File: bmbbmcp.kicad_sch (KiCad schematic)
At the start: 20 parts, among them J1 USB_OTG, J2 Conn_ARM_SWD_TagConnect_TC2030, J3 Conn_01x04_Socket, U1 MDBT50Q-1MV2, U2 AP2112K-3.3, Y1 32.768

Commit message: Adding parts and gerber files from JLCPCB plugin
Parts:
- C1, C6, C7: LCSC (none) -> C15850
- C2, C5: LCSC (none) -> C14663
- C3, C4: LCSC (none) -> C1653
- D1, D2: LCSC (none) -> C130880
- J1: LCSC (none) -> C136001
- R1: LCSC (none) -> C25804
- R2: LCSC (none) -> C23345
- S1, S2: LCSC (none) -> C99271
- U1: LCSC (none) -> C5118826
- U2: LCSC (none) -> C51118
- Y1: LCSC (none) -> C620155
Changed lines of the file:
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@@
 			)
 		)
+		(property "LCSC" "C14663"
+			(at 39.37 177.7999 0)
+			(effects
+				(font
+					(size 1.27 1.27)
+				)
+				(hide yes)
+			)
+		)
 		(pin "2"
 		)
@@
 			)
 		)
+		(property "LCSC" "C136001"
+			(at 156.21 125.73 0)
+			(effects
+				(font
+					(size 1.27 1.27)
+				)
+				(hide yes)
+			)
+		)
 		(pin "6"
 		)
@@
 			)
 		)
+		(property "LCSC" "C14663"
+			(at 52.07 177.7999 0)
+			(effects
+				(font
+					(size 1.27 1.27)
+				)
+				(hide yes)
+			)
+		)
 		(pin "2"
 		)
@@
 			)
 		)
+		(property "LCSC" "C25804"
+			(at 102.87 181.6099 0)
+			(effects
+				(font
+					(size 1.27 1.27)
+				)
+				(hide yes)
+			)
+		)
 		(pin "1"
 		)
@@
 			)
 		)
+		(property "LCSC" "C23345"
+			(at 170.18 133.604 0)
+			(effects
+				(font
+					(size 1.27 1.27)
+				)
+				(hide yes)
+			)
+		)
 		(pin "2"
 		)
@@
 			)
 		)
+		(property "LCSC" "C15850"
+			(at 91.44 181.6099 0)
+			(effects
+				(font
+					(size 1.27 1.27)
+				)
+				(hide yes)
+			)
+		)
 		(pin "1"
 		)
@@
 			)
 		)
+		(property "LCSC" "C99271"
+			(at 149.86 64.77 0)
+			(effects
+				(font
+					(size 1.27 1.27)
+				)
+				(hide yes)
+			)
+		)
 		(pin "2"
 		)
@@
 			)
 		)
+		(property "LCSC" "C99271"
+			(at 149.86 85.09 0)
+			(effects
+				(font
+					(size 1.27 1.27)
+				)
+				(hide yes)
+			)
+		)
 		(pin "2"
 		)
@@
 			)
 		)
+		(property "LCSC" "C15850"
+			(at 132.08 181.6099 0)
+			(effects
+				(font
+					(size 1.27 1.27)
+				)
+				(hide yes)
+			)
+		)
 		(pin "1"
 		)
@@
 			)
 		)
+		(property "LCSC" "C15850"
+			(at 26.67 177.7999 0)
+			(effects
+				(font
+					(size 1.27 1.27)
+				)
+				(hide yes)
+			)
+		)
 		(pin "1"
 		)
@@
 			)
 		)
+		(property "LCSC" "C1653"
+			(at 99.06 53.594 0)
+			(effects
+				(font
+					(size 1.27 1.27)
+				)
+				(hide yes)
+			)
+		)
 		(pin "1"
 		)
@@
 			)
 		)
+		(property "LCSC" "C1653"
+			(at 98.806 35.306 0)
+			(effects
+				(font
+					(size 1.27 1.27)
+				)
+				(hide yes)
+			)
+		)
 		(pin "1"
 		)
@@
 			)
 		)
+		(property "LCSC" "C130880"
+			(at 81.5975 170.18 0)
+			(effects
+				(font
+					(size 1.27 1.27)
+				)
+				(hide yes)
+			)
+		)
 		(pin "1"
 		)
@@
 			)
 		)
+		(property "LCSC" "C620155"
+			(at 87.376 37.592 0)
+			(effects
+				(font
+					(size 1.27 1.27)
+				)
+				(hide yes)
+			)
+		)
 		(pin "1"
 		)
@@
 			)
 		)
+		(property "LCSC" "C130880"
+			(at 90.17 169.2274 0)
+			(effects
+				(font
+					(size 1.27 1.27)
+				)
+				(hide yes)
+			)
+		)
 		(pin "1"
 		)
@@
 			)
 		)
+		(property "LCSC" "C5118826"
+			(at 61.8841 125.73 0)
+			(effects
+				(font
+					(size 1.27 1.27)
+				)
+				(hide yes)
+			)
+		)
 		(pin "61"
 		)
@@
 			(effects
 				(font
+					(size 1.27 1.27)
+				)
+				(hide yes)
+			)
+		)
+		(property "LCSC" "C51118"
+			(at 116.84 170.18 0)
+			(effects
+				(font

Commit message: Initial full board design
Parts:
- removed J3: Conn_01x04_Socket, Connector_PinHeader_2.00mm:PinHeader_1x04_P2.00mm_Vertical, symbol Connector:Conn_01x04_Socket
- added J3: Conn_01x12_Socket, Connector_PinHeader_2.54mm:PinHeader_1x12_P2.54mm_Vertical, symbol Connector:Conn_01x12_Socket
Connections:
- net +3.3V: now also J3.2 (Pin_2)
- net +BATT: now also J3.1 (Pin_1)
- net GND: now also J3.4 (Pin_4)
- net MOTOR_B2: now reaches U1.11 (P0.02)
- net MOTOR_B1: now reaches U1.12 (P0.31)
- net MOTOR_A2: now reaches U1.13 (P0.28)
- net MOTOR_A1: now reaches U1.14 (P0.30)
- net I2S_MODE: now reaches U1.19 (P0.26)
- net BTN1: now reaches U1.20 (P0.04)
- net BTN1: now also J3.3 (Pin_3)
- net I2S_DOUT: now reaches U1.21 (P0.05)
- net I2S_LRCK: now reaches U1.23 (P0.07)
- net I2S_SCK: now reaches U1.25 (P1.08)
- net SPI_SCLK: now reaches U1.37 (P0.13)
- net SPI_MOSI: now reaches U1.39 (P0.15)
- net SPI_MISO: now reaches U1.44 (P0.20)
- net SPI_CS1: now reaches U1.50 (P1.02)
- net MOTOR_CTRL: now reaches U1.61 (P1.01)
- no-connect marks 49 -> 42
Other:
- added sheet components (components.kicad_sch)
- note added: "nRF2840 and power"

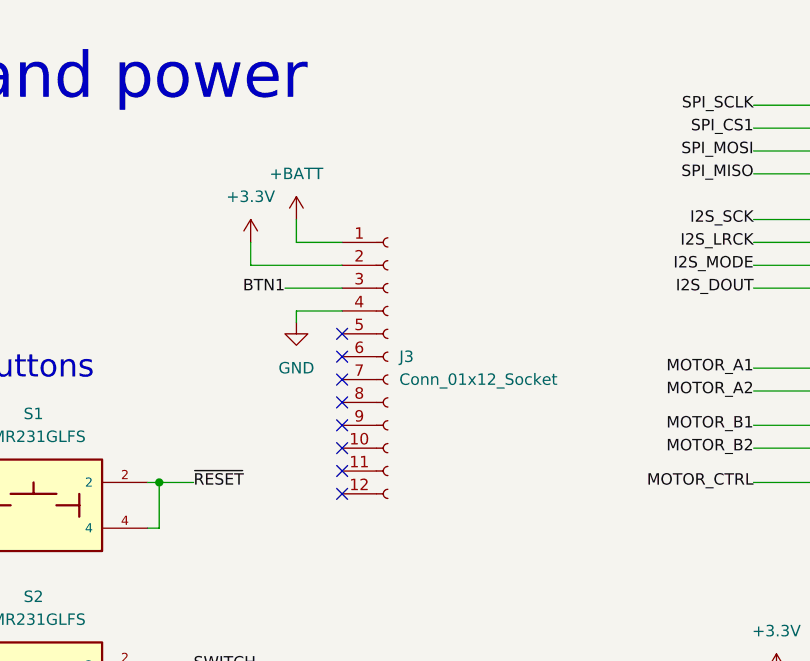
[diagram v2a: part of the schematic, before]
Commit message: Switch to three pin
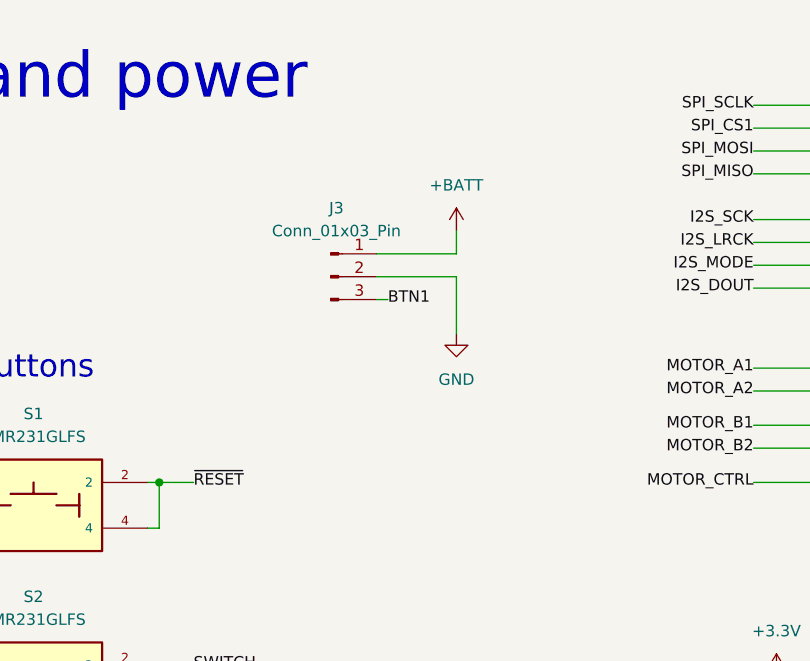
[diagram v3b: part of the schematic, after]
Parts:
- removed J3: Conn_01x12_Socket, Connector_PinHeader_2.54mm:PinHeader_1x12_P2.54mm_Vertical, symbol Connector:Conn_01x12_Socket
- added J3: Conn_01x03_Pin, Connector_PinHeader_2.54mm:PinHeader_1x03_P2.54mm_Vertical, symbol Connector:Conn_01x03_Pin
- R3: LCSC (none) -> C23345
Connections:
- net +BATT: now also J3.1 (Pin_1)
- net BTN1: now also J3.3 (Pin_3)
- net GND: now also J3.2 (Pin_2)
- no-connect marks 42 -> 34

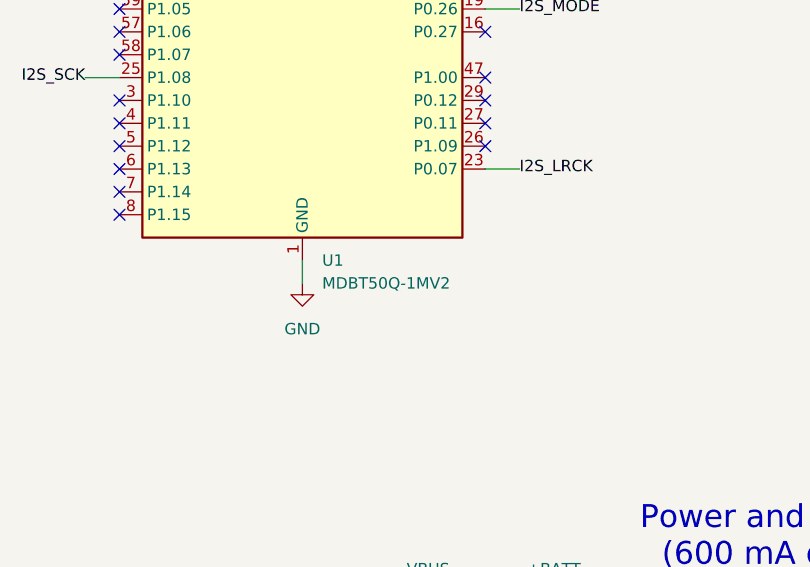
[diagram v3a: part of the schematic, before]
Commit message: Switch MCU from MDBT50Q-1MV2 to MDBT50Q-P1MV2 (PCB antenna version, in stock)
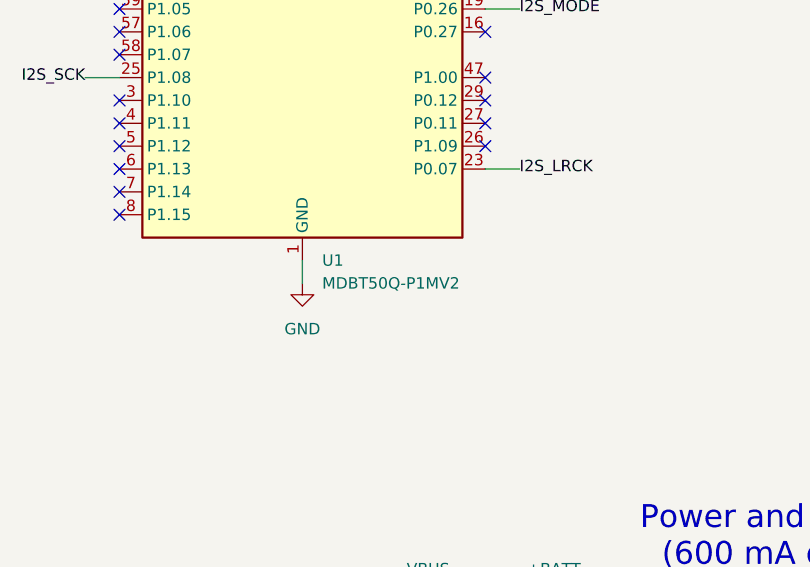
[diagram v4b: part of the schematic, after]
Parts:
- U1: value MDBT50Q-1MV2 -> MDBT50Q-P1MV2; symbol RF_Module:MDBT50Q-1MV2 -> RF_Module:MDBT50Q-P1MV2
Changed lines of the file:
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@@
 	)
 	(symbol
-		(lib_id "RF_Module:MDBT50Q-1MV2")
+		(lib_id "RF_Module:MDBT50Q-P1MV2")
 		(at 59.69 80.01 0)
 		(unit 1)
@@
 			)
 		)
-		(property "Value" "MDBT50Q-1MV2"
+		(property "Value" "MDBT50Q-P1MV2"
 			(at 61.8841 128.27 0)
 			(effects
